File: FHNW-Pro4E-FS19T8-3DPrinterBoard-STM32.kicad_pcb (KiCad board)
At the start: 4 copper layers, 158 x 95 mm, 221 parts, among them J101 Screw_Terminal_01x02, J201 Micro_SD_Card_Det, J202 Conn_02x05_Odd_Even, J203 Conn_02x20_Odd_Even, J204 Conn_ARM_JTAG_SWD_10, J401 Conn_01x02, J402 Conn_01x02, J403 Screw_Terminal_01x02, J404 Conn_01x02, J405 Conn_01x02, J406 Screw_Terminal_01x02, J407 Conn_01x02, J408 Conn_01x02, J409 Conn_01x02, J410 Conn_01x02, J411 Conn_01x02, J504 USB_C_Receptacle, J601 B4B-XH-A, J602 B4B-XH-A, J603 B4B-XH-A, J604 B4B-XH-A, Q1 2N3904, Q2 2N3904, SW201 SW_Push, SW301 SW_Push, SW302 SW_Push, T101 BUK963R3-60E, T401 PMV40UN2, T402 BUK963R3-60E, T403 BUK963R3-60E, T404 PMV40UN2, T405 PMV40UN2, U1 USBLC6-2SC6, U101 LM2675M-3.3, U102 LM2675M-5, U201 STM32F103ZETx, U202 NTS0104PW-Q100J, U203 NTS0104PW-Q100J, U301 ESP32-WROOM-32, U502 FT2232D, U601 TMC2660, U602 TMC2660, U603 TMC2660, U604 TMC2660, X201 SG-210STF, X501 SG5032CCN-6.000000M-HJGA3

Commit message: first layout draft without 40pin
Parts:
- added D106: APHBM2012LSURKZGKC, FHNW-Pro4E-FS19T8-Library:LED_Kingbright_SMD4_2.0x1.25, F.Cu at (85.2, 79.4)
- added R104: 10k, Resistors_SMD:R_1206, F.Cu at (85.2, 75.3)
- moved C106 87.1 mm to (174.2, 81.3), turned to 270 degrees
- moved FB102 86.7 mm to (175.9, 80.5)
- moved FB101 65.5 mm to (186.9, 38.4), turned to 0 degrees
- moved J504 55.3 mm to (210.1, 111.1), turned to 0 degrees
- moved J203 55.2 mm to (236.9, 103.5), turned to 180 degrees
- moved R216 51.2 mm to (182.2, 106.0), turned to 90 degrees
- moved C203 50.4 mm to (183.5, 106.0), turned to 90 degrees
- moved C502 50.4 mm to (204.3, 108.8), turned to 90 degrees
- moved C105 50.0 mm to (186.6, 6.60), turned to 180 degrees
- moved D504 48.3 mm to (221.6, 99.7), turned to 270 degrees
- moved J201 46.8 mm to (191.5, 106.2), turned to 0 degrees
- moved D505 46.4 mm to (219.1, 99.7), turned to 270 degrees
- moved D502 44.6 mm to (216.5, 99.7), turned to 270 degrees
- moved J202 44.2 mm to (225.4, 60.3), turned to 270 degrees
- moved U1 42.8 mm to (210.1, 101.7), turned to 270 degrees
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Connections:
- net Net-(C110-Pad1) renamed /24V_IN
- net Net-(J101-Pad1) renamed /24V_GND
- C401 pad 1: /ADC_T_BED -> /appendix_SENSORS_POWER/ADC_TEMP_BED
- C402 pad 1: /SW_Min_X -> /appendix_SENSORS_POWER/SW_End_X
- C403 pad 1: /ADC_T_E1 -> /appendix_SENSORS_POWER/ADC_TEMP_E1
- C404 pad 1: /SW_Min_Y -> /appendix_SENSORS_POWER/SW_End_Y
- C405 pad 1: /SW_End_Filament1 -> /appendix_SENSORS_POWER/SW_End_Filament_1
- C406 pad 1: /SW_Min_Z -> /appendix_SENSORS_POWER/SW_End_Z
- C407 pad 1: /ADC_T_PCB -> /appendix_SENSORS_POWER/ADC_TEMP_PCB
- J402 pad 1: /SW_Min_X -> /appendix_SENSORS_POWER/SW_End_X
- J404 pad 1: /ADC_T_BED -> /appendix_SENSORS_POWER/ADC_TEMP_BED
- J405 pad 1: /SW_Min_Y -> /appendix_SENSORS_POWER/SW_End_Y
- J407 pad 1: /ADC_T_E1 -> /appendix_SENSORS_POWER/ADC_TEMP_E1
- J408 pad 1: /SW_Min_Z -> /appendix_SENSORS_POWER/SW_End_Z
- J410 pad 1: /SW_End_Filament1 -> /appendix_SENSORS_POWER/SW_End_Filament_1
- R401 pad 2: /ADC_T_BED -> /appendix_SENSORS_POWER/ADC_TEMP_BED
- R402 pad 2: /SW_Min_X -> /appendix_SENSORS_POWER/SW_End_X
- R404 pad 2: /FAN1 -> /appendix_STM32F103/FAN1
- R405 pad 2: /ADC_T_E1 -> /appendix_SENSORS_POWER/ADC_TEMP_E1
- R406 pad 2: /SW_Min_Y -> /appendix_SENSORS_POWER/SW_End_Y
- R407 pad 2: /BED_ON -> /appendix_STM32F103/BED_ON
- R409 pad 2: /SW_End_Filament1 -> /appendix_SENSORS_POWER/SW_End_Filament_1
- R410 pad 2: /SW_Min_Z -> /appendix_SENSORS_POWER/SW_End_Z
- R411 pad 2: /E1_ON -> /appendix_STM32F103/E1_ON
- R413 pad 2: /FAN2 -> /appendix_STM32F103/FAN2
- R415 pad 2: /ADC_T_PCB -> /appendix_SENSORS_POWER/ADC_TEMP_PCB
- R416 pad 2: /E1_ON -> /appendix_STM32F103/E1_ON
- R417 pad 2: /BED_ON -> /appendix_STM32F103/BED_ON
- R418 pad 1: /FAN1 -> /appendix_STM32F103/FAN1
- R419 pad 1: /FAN2 -> /appendix_STM32F103/FAN2
- R420 pad 2: /FAN3 -> /appendix_STM32F103/FAN3
- R421 pad 1: /FAN3 -> /appendix_STM32F103/FAN3
- R422 pad 1: /E1_ON -> /appendix_STM32F103/E1_ON
- R423 pad 1: /BED_ON -> /appendix_STM32F103/BED_ON
- TH401 pad 2: /ADC_T_PCB -> /appendix_SENSORS_POWER/ADC_TEMP_PCB
- U201 pad 101: /appendix_UART_USB/FT_RX_A -> /appendix_ESP32/ESP_RX_STM
- U201 pad 102: /appendix_UART_USB/FT_TX_A -> /appendix_ESP32/ESP_TX_STM
- U201 pad 11: /appendix_STM32F103/CS_X -> /appendix_SENSORS_POWER/SW_End_X
- U201 pad 12: /appendix_STM32F103/EN_X -> /appendix_SENSORS_POWER/SW_End_Y
- U201 pad 13: /appendix_STM32F103/STALL_X -> /appendix_STM32F103/FAN1
- U201 pad 14: /appendix_STM32F103/DIR_X -> /appendix_STM32F103/FAN2
- U201 pad 15: /appendix_STM32F103/STEP_X -> /appendix_STM32F103/FAN3
- U201 pad 28: /appendix_STM32F103/ADC_T_BED -> /appendix_SENSORS_POWER/ADC_TEMP_E1
- U201 pad 29: /appendix_STM32F103/ADC_T_E1 -> /appendix_SENSORS_POWER/ADC_TEMP_BED
- U201 pad 3: Net-(U201-Pad3) -> /appendix_SENSORS_POWER/SW_End_Filament_1
- U201 pad 35: Net-(U201-Pad35) -> /appendix_SENSORS_POWER/ADC_TEMP_PCB
- U201 pad 36: /appendix_ESP32/ESP_RX_STM -> /appendix_UART_USB/FT_RX_A
- U201 pad 37: /appendix_ESP32/ESP_TX_STM -> /appendix_UART_USB/FT_TX_A
- U201 pad 4: Net-(U201-Pad4) -> /appendix_SENSORS_POWER/SW_End_Z
- U201 pad 41: Net-(U201-Pad41) -> /appendix_STM32F103/STEP_X
- U201 pad 42: Net-(U201-Pad42) -> /appendix_STM32F103/DIR_X
- U201 pad 43: Net-(U201-Pad43) -> /appendix_STM32F103/STALL_X
- U201 pad 49: Net-(U201-Pad49) -> /appendix_STM32F103/EN_X
- U201 pad 50: Net-(U201-Pad50) -> /appendix_STM32F103/CS_X
- U201 pad 69: Net-(U201-Pad69) -> /appendix_STM32F103/E1_ON
- U202 pad 8: +5V -> +3V3
- U203 pad 8: +5V -> +3V3
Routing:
- net /BED_ON: track 89.2 -> 0.00 mm
- net /appendix_STM32F103/BED_ON: track 2.52 -> 91.6 mm
- net /appendix_SENSORS_POWER/SW_End_Y: track 0.00 -> 87.4 mm
- net /appendix_STM32F103/FAN3: track 0.00 -> 84.1 mm
- net /appendix_STM32F103/FAN2: track 0.00 -> 76.5 mm
- net /appendix_UART_USB/FT_TX_A: track 4.99 -> 79.4 mm
- net /appendix_STM32F103/E1_ON: track 0.00 -> 72.6 mm
- net /appendix_SENSORS_POWER/SW_End_X: track 0.00 -> 71.0 mm
- net /E1_ON: track 69.7 -> 0.00 mm
- net /appendix_UART_USB/FT_RX_A: track 5.02 -> 74.6 mm
- net /appendix_STM32F103/FAN1: track 0.00 -> 69.0 mm
- net /appendix_SENSORS_POWER/SW_End_Z: track 0.00 -> 63.9 mm
- net +3.3VA: track 13.7 -> 77.5 mm, vias 2 -> 4
- net MISO: track 185.7 -> 249.3 mm, vias 5 -> 6
- net SCK: track 191.9 -> 250.9 mm
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
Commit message: user LED + fixes in Layout
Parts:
- added D202: LED, LED_SMD:LED_0805_2012Metric, F.Cu at (152.4, 40.0)
- added D203: LED, LED_SMD:LED_0805_2012Metric, F.Cu at (181.0, 99.7)
- added G101: SYM_Serial_No, FHNW-Pro4E-FS19T8-Library:Label_Serial_Number_6x20, F.Cu at (85.3, 95.9)
- added G102: SYM_FHNW_Logo, FHNW-Pro4E-FS19T8-Library:Logo_FHNW_03x05mm, F.Cu at (230.8, 102.1)
- added LOGO101: OSHW-LOGOM-COPPER, Symbols:OSHW-Logo2_9.8x8mm_SilkScreen, F.Cu at (224.8, 110.5)
- added R218: 330R, Resistors_SMD:R_0603, F.Cu at (155.6, 40.0)
- added R219: 330R, Resistors_SMD:R_0603, F.Cu at (181.0, 96.5)
- D105: value D_Zener -> BZT52H-B7V5; footprint Diodes_SMD:D_SMB -> Diodes_SMD:D_SOD-123
- moved D201 12.9 mm to (152.4, 37.5)
- moved R202 12.7 mm to (155.6, 37.5), turned to 180 degrees
- moved J203 1.27 mm to (236.9, 104.8)
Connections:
- net Net-(U202-Pad4) renamed LCD_Reset
- D201 pad 1: Net-(D201-Pad1) -> GND
- R202 pad 1: Net-(R202-Pad1) -> LED_USER_1
- U201 pad 1: Net-(U201-Pad1) -> LCD_ENC_BTN
- U201 pad 103: Net-(U201-Pad103) -> SD_DETECT
- U201 pad 104: Net-(U201-Pad104) -> LED_Marlin
- U201 pad 139: Net-(U201-Pad139) -> LCD_CS
- U201 pad 140: Net-(U201-Pad140) -> LCD_ENC_B
- U201 pad 141: Net-(U201-Pad141) -> LCD_ENC_A
- U201 pad 142: Net-(U201-Pad142) -> LCD_BUZZER
- U201 pad 45: Net-(U201-Pad45) -> LED_USER_1
- U201 pad 46: Net-(U201-Pad46) -> LED_USER_2
- U202 pad 2: Net-(U202-Pad2) -> MOSI
- U202 pad 3: Net-(U202-Pad3) -> SCK
- U202 pad 5: Net-(U202-Pad5) -> LCD_ENC_BTN
- U203 pad 2: Net-(U203-Pad2) -> LCD_BUZZER
- U203 pad 3: Net-(U203-Pad3) -> LCD_ENC_A
- U203 pad 4: Net-(U203-Pad4) -> LCD_ENC_B
- U203 pad 5: Net-(U203-Pad5) -> LCD_CS
- U601 pad 15: SCK -> MOSI
- U601 pad 16: MOSI -> SCK
- U602 pad 15: SCK -> MOSI
- U602 pad 16: MOSI -> SCK
- U603 pad 15: SCK -> MOSI
- U603 pad 16: MOSI -> SCK
- U604 pad 15: SCK -> MOSI
- U604 pad 16: MOSI -> SCK
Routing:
- net SCK: track 250.9 -> 328.3 mm, vias 6 -> 7
- net MOSI: track 246.1 -> 319.2 mm, vias 6 -> 7
- net LED_Marlin: track 0.00 -> 31.6 mm
- net SD_DETECT: track 20.4 -> 48.5 mm
- net Net-(U201-Pad96): track 2.17 -> 28.8 mm, vias 0 -> 1
- net LCD_CS: track 0.00 -> 25.9 mm
- net Net-(U201-Pad97): track 2.09 -> 27.7 mm, vias 0 -> 1
- net LCD_ENC_B: track 0.00 -> 25.4 mm
- net LED_USER_2: track 0.00 -> 25.3 mm, vias 0 -> 2
- net LCD_ENC_A: track 0.00 -> 25.0 mm
- net LED_USER_1: track 0.00 -> 24.8 mm, vias 0 -> 2
- net LCD_BUZZER: track 0.00 -> 24.5 mm
- net LCD_ENC_BTN: track 0.00 -> 23.1 mm
- net LCD_Reset: track 0.00 -> 22.4 mm
- net GND: track 376.0 -> 392.5 mm, vias 96 -> 97
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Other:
- board text added: "EXT3"
- board text added: "LED MARLIN"
- board text added: "LED1"
- board text added: "LED2"
- board text added: "RX"
- board text added: "TX"
- board text added: "University of Applied Sciences Northwestern Switzerland"

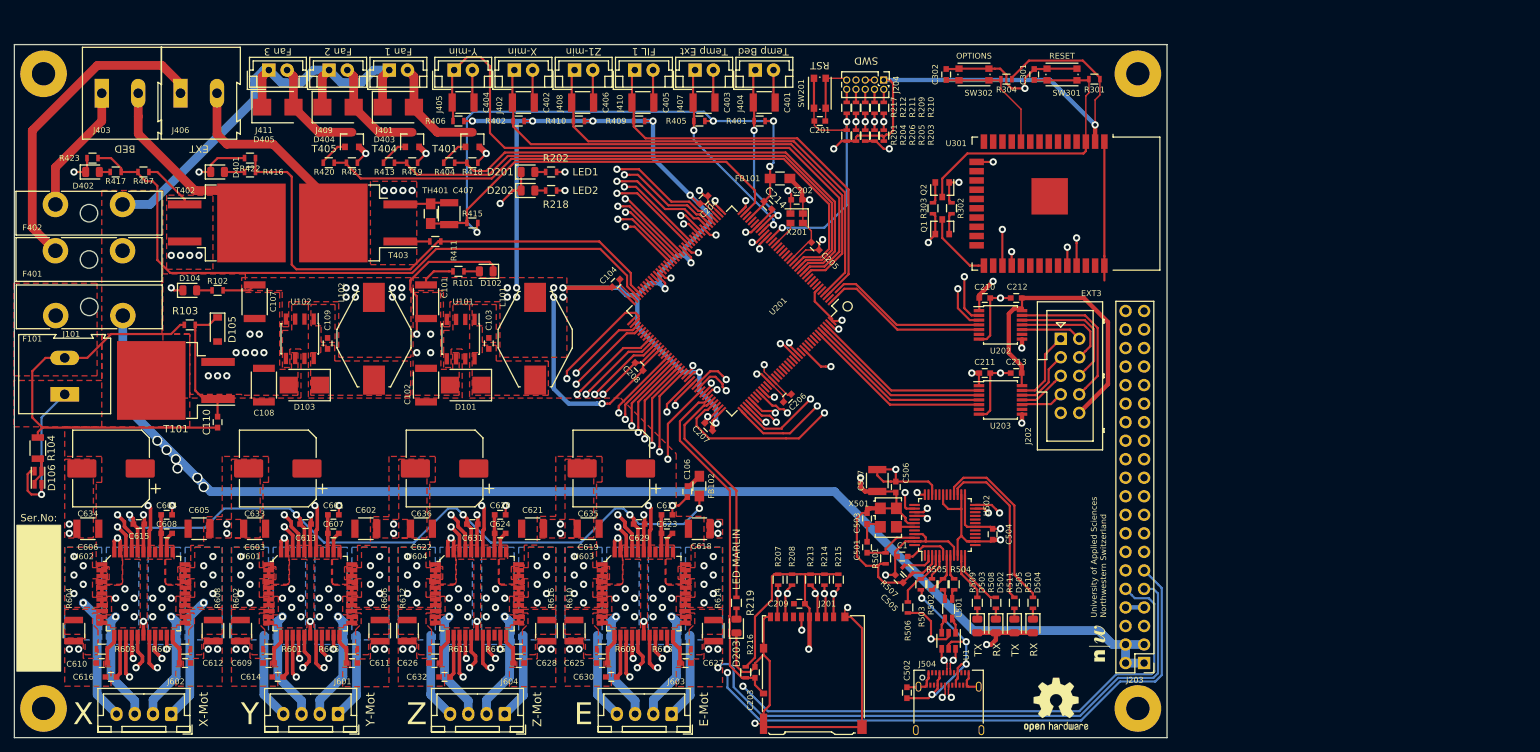
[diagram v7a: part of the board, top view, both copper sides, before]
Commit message: TVS protection, BOOT1 pin, user BTN
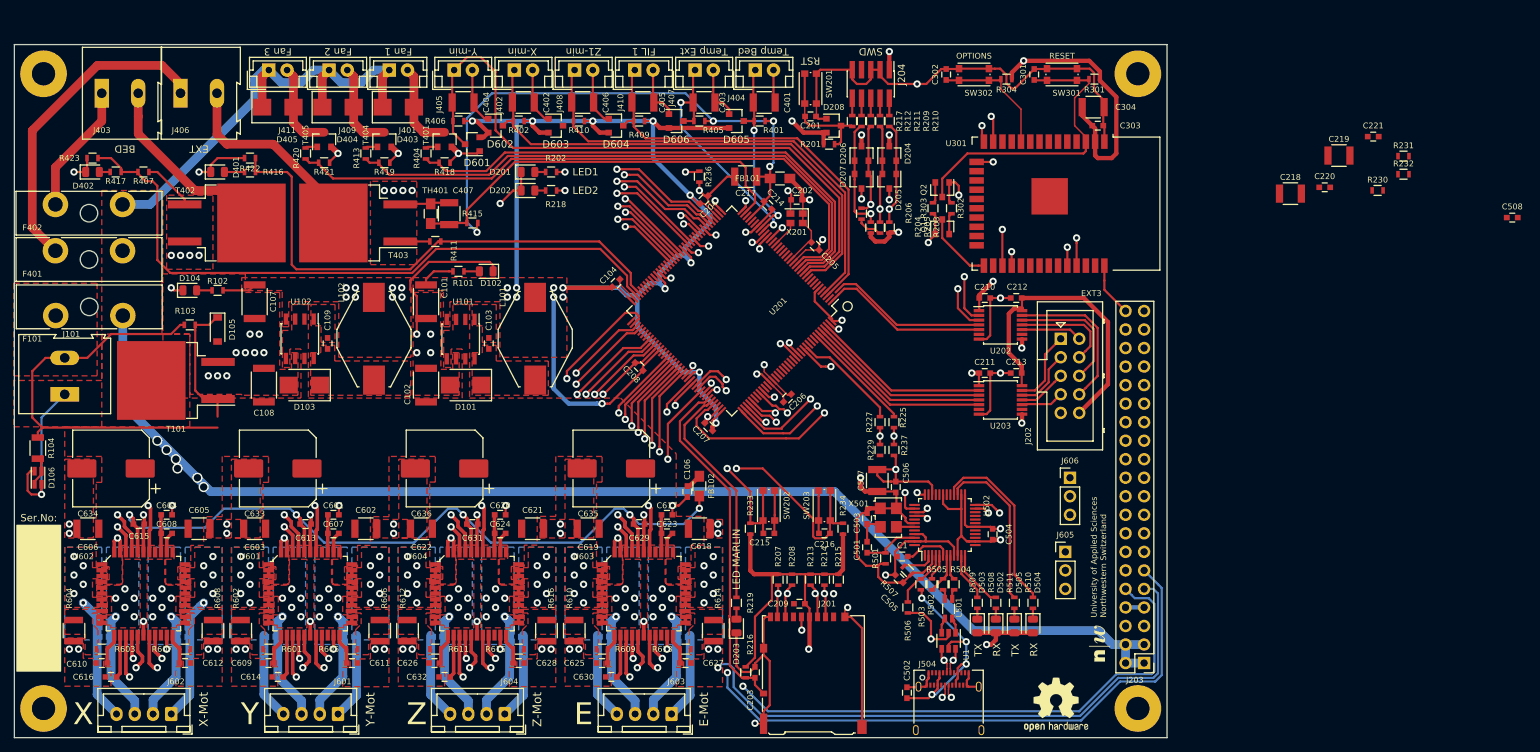
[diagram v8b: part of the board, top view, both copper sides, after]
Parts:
- removed C110: TBD, Capacitors_SMD:C_0603
- added C215: 100n, Capacitors_SMD:C_0603, F.Cu at (185.4, 87.0)
- added C216: 100n, Capacitors_SMD:C_0603, F.Cu at (193.0, 87.0)
- added C217: 10u, Capacitors_SMD:C_1210, F.Cu at (182.2, 38.1)
- added C218: 10u, Capacitors_SMD:C_1210, F.Cu at (256.9, 40.4)
- added C219: 10u, Capacitors_SMD:C_1210, F.Cu at (263.6, 35.2)
- added C220: 100n, Capacitors_SMD:C_0603, F.Cu at (261.6, 39.6)
- added C221: 100n, Capacitors_SMD:C_0603, F.Cu at (268.3, 32.6)
- added C303: 100n, Capacitors_SMD:C_0603, F.Cu at (230.5, 31.1)
- added C304: 10u, Capacitors_SMD:C_1210, F.Cu at (229.9, 28.6)
- added C508: 100n, Capacitors_SMD:C_0603, F.Cu at (287.3, 43.7)
- added D204: BAT54C, Package_TO_SOT_SMD:SOT-23, F.Cu at (201.9, 34.9)
- added D205: BAT54A, Package_TO_SOT_SMD:SOT-23, F.Cu at (201.9, 38.7)
- added D206: BAT54C, Package_TO_SOT_SMD:SOT-23, F.Cu at (198.1, 34.9)
- added D207: BAT54A, Package_TO_SOT_SMD:SOT-23, F.Cu at (198.1, 38.7)
- added D208: BAT54S, Package_TO_SOT_SMD:SOT-23, F.Cu at (194.3, 31.1)
- added D601: BAT54S, Package_TO_SOT_SMD:SOT-23, F.Cu at (148.0, 31.1)
- added D602: BAT54S, Package_TO_SOT_SMD:SOT-23, F.Cu at (144.8, 33.7)
- added D603: BAT54S, Package_TO_SOT_SMD:SOT-23, F.Cu at (156.2, 31.1)
- added D604: BAT54S, Package_TO_SOT_SMD:SOT-23, F.Cu at (164.5, 31.1)
- added D605: BAT54S, Package_TO_SOT_SMD:SOT-23, F.Cu at (181.0, 30.5)
- added D606: BAT54S, Package_TO_SOT_SMD:SOT-23, F.Cu at (172.7, 30.5)
- added J605: Conn_01x03, Connector_PinHeader_2.54mm:PinHeader_1x03_P2.54mm_Vertical, F.Cu at (226.1, 89.5)
- added J606: Conn_01x03, Connector_PinHeader_2.54mm:PinHeader_1x03_P2.54mm_Vertical, F.Cu at (226.7, 79.4)
- added R225: 0R, Resistors_SMD:R_0603, F.Cu at (202.6, 71.8)
- added R227: 0R, Resistors_SMD:R_0603, F.Cu at (200.7, 71.8)
- added R229: 0R, Resistors_SMD:R_0603, F.Cu at (200.7, 75.6)
- added R230: 10k, Resistors_SMD:R_0603, F.Cu at (268.9, 40.0)
- added R231: 10k, Resistors_SMD:R_0603, F.Cu at (272.4, 35.3)
- added R232: 10k, Resistors_SMD:R_0603, F.Cu at (272.4, 37.8)
- added R233: 10k, Resistors_SMD:R_0603, F.Cu at (182.9, 86.4)
- added R234: 10k, Resistors_SMD:R_0603, F.Cu at (195.6, 86.4)
- added R236: 10k, Resistors_SMD:R_0603, F.Cu at (175.9, 38.1)
- added R237: 10k, Resistors_SMD:R_0603, F.Cu at (202.6, 75.6)
- added SW202: SW_Push, Buttons_Switches_SMD:SW_SPST_KMR2, F.Cu at (185.4, 83.2)
- added SW203: SW_Push, Buttons_Switches_SMD:SW_SPST_KMR2, F.Cu at (193.0, 83.2)
- C202, C203: value 10n -> 100n
- C214: value 100n -> 10n
- J204: footprint Connector_PinHeader_1.27mm:PinHeader_2x05_P1.27mm_Vertical -> Connector_PinHeader_1.27mm:PinHeader_2x05_P1.27mm_Vertical_SMD
- R103: value TBD -> 100k
- R209, R210, R211, R212, R217: value 200R -> 100R
- SW201, SW301, SW302: footprint Button_Switch_SMD:SW_SPST_KMR2 -> Buttons_Switches_SMD:SW_SPST_KMR2
- moved R204 12.8 mm to (199.4, 45.1)
- moved R203 12.6 mm to (201.9, 45.1)
- moved R205 12.6 mm to (200.7, 45.1)
- moved R206 10.7 mm to (198.1, 43.2)
- moved R421 3.81 mm to (124.5, 36.2)
- moved T405 3.81 mm to (124.5, 33.0)
- moved R418 3.81 mm to (141.0, 36.2)
- moved R419 3.81 mm to (132.7, 36.2)
- moved T401 3.81 mm to (141.0, 33.0)
- moved T404 3.81 mm to (132.7, 33.0)
- moved R420 3.42 mm to (121.9, 34.9), turned to 270 degrees
- moved R404 3.42 mm to (138.4, 34.9), turned to 270 degrees
- moved R413 3.42 mm to (130.2, 34.9), turned to 270 degrees
- moved R201 2.69 mm to (193.7, 33.7), turned to 0 degrees
- moved R210 1.96 mm to (201.9, 30.5)
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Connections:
- U201 pad 134: JTAG_TRST -> NRST
- U201 pad 138: /appendix_STM32F103/STM_BOOT1 -> /appendix_STM32F103/STM_BOOT0
- U201 pad 96: Net-(U201-Pad96) -> BTN_USER_1
- U201 pad 97: Net-(U201-Pad97) -> BTN_USER_2
- U301 pad 13: Net-(U301-Pad13) -> /appendix_STM32F103/STM32_NRST
- U301 pad 14: Net-(U301-Pad14) -> /appendix_STM32F103/STM32_BOOT_0
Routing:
- net +3V3: track 605.7 -> 695.0 mm, vias 31 -> 35
- net /appendix_STM32F103/STM32_NRST: track 0.00 -> 58.2 mm, vias 0 -> 2
- net /appendix_STM32F103/STM32_BOOT_0: track 0.00 -> 53.6 mm, vias 0 -> 2
- net GND: track 392.5 -> 441.7 mm, vias 97 -> 98
- net BTN_USER_2: track 0.00 -> 42.5 mm, vias 0 -> 2
- net BTN_USER_1: track 0.00 -> 33.7 mm, vias 0 -> 2
- net Net-(U201-Pad96): track 28.8 -> 0.00 mm, vias 1 -> 0
- net Net-(U201-Pad97): track 27.7 -> 0.00 mm, vias 1 -> 0
- net JTAG_RESET: track 37.3 -> 18.8 mm, vias 2 -> 1
- net /appendix_STM32F103/STM_BOOT1: track 0.00 -> 16.5 mm, vias 0 -> 2
- net /appendix_STM32F103/STM_BOOT0: track 0.00 -> 15.4 mm
- net NRST: track 0.00 -> 14.7 mm
- net JTAG_TDO_SWO: track 48.8 -> 42.0 mm
- net /appendix_SENSORS_POWER/ADC_TEMP_E1: track 27.8 -> 34.2 mm
- net SD_DAT2: track 49.1 -> 44.4 mm
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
